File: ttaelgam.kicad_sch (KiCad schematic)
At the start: 32 parts, among them J1 Conn_01x04, J2 USB_C_Receptacle_USB2.0_16P, J3 Conn_01x05, SW1 SW_Push, SW2 SW_Push, U1 RP2040, U2 XC6206PxxxMR, U3 SRV05-4, U4 W25Q128JVS, Y1 Crystal_GND24

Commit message: 202408042026
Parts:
- added D1, D10, D11, D12, D13, D14, D15, D16, D17, D18, D19, D2, D20, D21, D22, D23, D24, D25, D26, D27, D28, D29, D3, D30, D31, D32, D33, D34, D35, D36, D37, D38, D39, D4, D40, D41, D42, D43, D44, D45, D46, D47, D48, D49, D5, D50, D51, D52, D53, D54, D55, D56, D57, D58, D59, D6, D60, D61, D62, D63, D64, D65, D66, D67, D68, D69, D7, D70, D71, D72, D73, D74, D75, D76, D77, D78, D79, D8, D80, D81, D82, D83, D84, D85, D86, D87, D88, D89, D9, D90: D_Small, Diode_SMD:D_SOD-123, symbol Device:D_Small
- added MX1, MX10, MX11, MX12, MX13, MX14, MX15, MX16, MX17, MX18, MX19, MX2, MX20, MX21, MX22, MX23, MX24, MX25, MX26, MX27, MX28, MX29, MX3, MX30, MX31, MX32, MX33, MX34, MX35, MX36, MX37, MX38, MX39, MX4, MX40, MX41, MX42, MX43, MX44, MX45, MX46, MX47, MX48, MX49, MX5, MX50, MX51, MX52, MX53, MX54, MX55, MX56, MX57, MX58, MX59, MX6, MX60, MX61, MX62, MX63, MX64, MX65, MX66, MX67, MX68, MX69, MX7, MX70, MX71, MX72, MX73, MX74, MX75, MX76, MX77, MX78, MX79, MX8, MX80, MX81, MX82, MX83, MX84, MX85, MX86, MX87, MX88, MX89, MX9, MX90: MX_SW_HS, marbastlib-mx:SW_MX_HS_CPG151101S11_1u, symbol marbastlib-mx:MX_SW_HS_CPG151101S11
- BOOT1: renamed from SW2; footprint (none) -> Button_Switch_SMD:SW_SPST_TL3342
- C1, C2: footprint (none) -> Capacitor_SMD:C_0402_1005Metric
- C10: renamed from C7; footprint (none) -> Capacitor_SMD:C_0402_1005Metric
- C11: renamed from C8; footprint (none) -> Capacitor_SMD:C_0402_1005Metric
- C12: renamed from C9; footprint (none) -> Capacitor_SMD:C_0402_1005Metric
- C3: renamed from C4; footprint (none) -> Capacitor_SMD:C_0402_1005Metric
- C4: renamed from C5; footprint (none) -> Capacitor_SMD:C_0402_1005Metric
- C5: renamed from C12; footprint (none) -> Capacitor_SMD:C_0402_1005Metric
- C6: renamed from C10; footprint (none) -> Capacitor_SMD:C_0402_1005Metric
- C7: renamed from C11; footprint (none) -> Capacitor_SMD:C_0402_1005Metric
- C8: renamed from C3; footprint (none) -> Capacitor_SMD:C_0603_1608Metric
- C9: renamed from C6; footprint (none) -> Capacitor_SMD:C_0402_1005Metric
- F1: renamed from F2; footprint (none) -> Fuse:Fuse_1206_3216Metric
- J1: renamed from J2; footprint (none) -> Connector_USB:USB_C_Receptacle_HRO_TYPE-C-31-M-12
- J2: renamed from J1; footprint (none) -> Connector_JST:JST_SH_SM04B-SRSS-TB_1x04-1MP_P1.00mm_Horizontal
- J3: footprint (none) -> Connector_PinHeader_2.54mm:PinHeader_1x05_P2.54mm_Vertical
- R1: renamed from R2; footprint (none) -> Resistor_SMD:R_0402_1005Metric
- R2: renamed from R1; footprint (none) -> Resistor_SMD:R_0402_1005Metric
- R3: renamed from R9; footprint (none) -> Resistor_SMD:R_0402_1005Metric
- R4: renamed from R3; footprint (none) -> Resistor_SMD:R_0402_1005Metric
- R5: renamed from R8; footprint (none) -> Resistor_SMD:R_0402_1005Metric
- R6: renamed from R7; footprint (none) -> Resistor_SMD:R_0402_1005Metric
- R7: renamed from R4; footprint (none) -> Resistor_SMD:R_0402_1005Metric
- R8: renamed from R5; footprint (none) -> Resistor_SMD:R_0402_1005Metric
- R9: renamed from R6; footprint (none) -> Resistor_SMD:R_0402_1005Metric
- RST1: renamed from SW1; footprint (none) -> Button_Switch_SMD:SW_SPST_TL3342
- Y1: footprint (none) -> Crystal:Crystal_SMD_3225-4Pin_3.2x2.5mm
- renumbered U2 to U1, U1 to U2
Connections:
- new net: D13.2 (A), MX13.2
- new net: D31.2 (A), MX31.2
- new net: D46.2 (A), MX46.2
- new net: D73.2 (A), MX73.2
- new net: D89.2 (A), MX89.2
- new net: D74.2 (A), MX74.2
- new net: D64.2 (A), MX64.2
- new net: D24.2 (A), MX24.2
- new net: D47.2 (A), MX47.2
- new net: D69.2 (A), MX69.2
- new net: D32.2 (A), MX32.2
- new net: D56.2 (A), MX56.2
- new net: D17.2 (A), MX17.2
- new net: D14.2 (A), MX14.2
- new net: D16.2 (A), MX16.2
- new net: D15.2 (A), MX15.2
- new net: D41.2 (A), MX41.2
- new net: D5.2 (A), MX5.2
- new net: D68.2 (A), MX68.2
- new net: D52.2 (A), MX52.2
- new net: D85.2 (A), MX85.2
- new net: D70.2 (A), MX70.2
- new net: D53.2 (A), MX53.2
- new net: D7.2 (A), MX7.2
- new net: D61.2 (A), MX61.2
- new net: D75.2 (A), MX75.2
- new net: D34.2 (A), MX34.2
- new net: D9.2 (A), MX9.2
- new net: D4.2 (A), MX4.2
- new net: D49.2 (A), MX49.2
- new net: D66.2 (A), MX66.2
- new net: D21.2 (A), MX21.2
- new net: D30.2 (A), MX30.2
- new net: D50.2 (A), MX50.2
- new net: D72.2 (A), MX72.2
- new net: D62.2 (A), MX62.2
- new net: D20.2 (A), MX20.2
- new net: D39.2 (A), MX39.2
- new net: D54.2 (A), MX54.2
- new net: D11.2 (A), MX11.2
- new net: D88.2 (A), MX88.2
- new net: D10.2 (A), MX10.2
- new net: D80.2 (A), MX80.2
- new net: D82.2 (A), MX82.2
- new net: D43.2 (A), MX43.2
- new net: D48.2 (A), MX48.2
- new net: D3.2 (A), MX3.2
- new net: D40.2 (A), MX40.2
- new net: D37.2 (A), MX37.2
- new net: D83.2 (A), MX83.2
- new net: D38.2 (A), MX38.2
- new net: D29.2 (A), MX29.2
- new net: D55.2 (A), MX55.2
- new net: D8.2 (A), MX8.2
- new net: D33.2 (A), MX33.2
- new net: D86.2 (A), MX86.2
- new net: D23.2 (A), MX23.2
- new net: D44.2 (A), MX44.2
- new net: D63.2 (A), MX63.2
- new net: D28.2 (A), MX28.2
- new net: D60.2 (A), MX60.2
- new net: D26.2 (A), MX26.2
- new net: D58.2 (A), MX58.2
- new net: D77.2 (A), MX77.2
- new net: D76.2 (A), MX76.2
- new net: D57.2 (A), MX57.2
- new net: D45.2 (A), MX45.2
- new net: D2.2 (A), MX2.2
- new net: D84.2 (A), MX84.2
- new net: D35.2 (A), MX35.2
- new net: D59.2 (A), MX59.2
- new net: D90.2 (A), MX90.2
- new net: D71.2 (A), MX71.2
- new net: D18.2 (A), MX18.2
- new net: D6.2 (A), MX6.2
- new net: D12.2 (A), MX12.2
- new net: D67.2 (A), MX67.2
- new net: D36.2 (A), MX36.2
- new net: D78.2 (A), MX78.2
- new net: D19.2 (A), MX19.2
- new net: D79.2 (A), MX79.2
- new net: D42.2 (A), MX42.2
- new net: D25.2 (A), MX25.2
- new net: D1.2 (A), MX1.2
- new net: D65.2 (A), MX65.2
- new net: D27.2 (A), MX27.2
- new net: D51.2 (A), MX51.2
- new net: D81.2 (A), MX81.2
- new net: D87.2 (A), MX87.2
- new net: D22.2 (A), MX22.2
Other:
- moved on the sheet: C1, C10, C11, C12, C2, C8, C9, J2, U1, U3

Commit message: 0804over
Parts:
- added S30: MX_stab, marbastlib-mx:STAB_MX_2u, symbol marbastlib-mx:MX_stab
- added S63, S64: MX_stab, marbastlib-mx:STAB_MX_2.25u, symbol marbastlib-mx:MX_stab
- added S76, S81: MX_stab, marbastlib-mx:STAB_MX_2.75u, symbol marbastlib-mx:MX_stab
- added S82: MX_stab, marbastlib-mx:STAB_MX_3u, symbol marbastlib-mx:MX_stab
- MX34, MX47: footprint marbastlib-mx:SW_MX_HS_CPG151101S11_1u -> marbastlib-mx:SW_MX_HS_CPG151101S11_1.5u
- MX51: footprint marbastlib-mx:SW_MX_HS_CPG151101S11_1u -> marbastlib-mx:SW_MX_HS_CPG151101S11_1.75u_STP_1.25
- MX78, MX79, MX80, MX83: footprint marbastlib-mx:SW_MX_HS_CPG151101S11_1u -> marbastlib-mx:SW_MX_HS_CPG151101S11_1.25u

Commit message: 20240807
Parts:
- added C13, C14, C15, C16: 100n, Capacitor_SMD:C_0402_1005Metric, symbol Device:C_Small
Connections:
- net +1V1: now also C16.1
- net +3V3: now also C13.1, C14.1, C15.1
- net GND: now also J3.1 (Pin_1), C13.2, C14.2, C15.2, C16.2; no longer J3.3 (Pin_3)
- net Q_CLK: now also U4.6 (CLK); no longer U4.7 (IO3)
- net Q_I00: now also U4.5 (DI(IO0)); no longer U4.6 (CLK)
- net Q_I01: now also U4.2 (DO(IO1)); no longer U4.5 (DI(IO0))
- net Q_I02: now also U4.1 (~{CS}); no longer U4.2 (DO(IO1))
- net Q_I03: now also U4.7 (IO3); no longer U4.3 (IO2)
- net Q_SEL: now also U4.3 (IO2); no longer U4.1 (~{CS})
- net RESET: now also J3.3 (Pin_3); no longer J3.1 (Pin_1)
- net SWC: now also J3.5 (Pin_5); no longer J3.4 (Pin_4)
- net SWD: now also J3.4 (Pin_4); no longer J3.5 (Pin_5)
- net at MX13.1: now also MX30.1, MX47.1, MX63.1, MX76.1, MX87.1
- net at MX31.1: now also MX14.1, MX48.1, MX88.1
- net at D46.1 (K): now also D34.1 (K), D35.1 (K), D36.1 (K), D37.1 (K), D38.1 (K), D39.1 (K), D40.1 (K), D41.1 (K), D42.1 (K), D43.1 (K), D44.1 (K), D45.1 (K), D47.1 (K), D48.1 (K), D49.1 (K), D50.1 (K)
- net at MX73.1: now also MX27.1, MX43.1, MX60.1, MX9.1
- net at MX89.1: now also MX15.1, MX32.1, MX49.1, MX77.1
- net at MX74.1: now also MX10.1, MX28.1, MX44.1, MX61.1
- net at D64.1 (K): now also D65.1 (K), D66.1 (K), D67.1 (K), D68.1 (K), D69.1 (K), D70.1 (K), D71.1 (K), D72.1 (K), D73.1 (K), D74.1 (K), D75.1 (K), D76.1 (K), D77.1 (K)
- net at MX24.1: now also MX40.1, MX57.1, MX6.1, MX70.1, MX82.1
- net at MX69.1: now also MX23.1
- net at D32.1 (K): now also D17.1 (K), D18.1 (K), D19.1 (K), D20.1 (K), D21.1 (K), D22.1 (K), D23.1 (K), D24.1 (K), D25.1 (K), D26.1 (K), D27.1 (K), D28.1 (K), D29.1 (K), D30.1 (K), D31.1 (K), D33.1 (K)
- net at D56.1 (K): now also D51.1 (K), D52.1 (K), D53.1 (K), D54.1 (K), D55.1 (K), D57.1 (K), D58.1 (K), D59.1 (K), D60.1 (K), D61.1 (K), D62.1 (K), D63.1 (K)
- net at D16.1 (K): now also D1.1 (K), D10.1 (K), D11.1 (K), D12.1 (K), D13.1 (K), D14.1 (K), D15.1 (K), D2.1 (K), D3.1 (K), D4.1 (K), D5.1 (K), D6.1 (K), D7.1 (K), D8.1 (K), D9.1 (K)
- net at D85.1 (K): now also D78.1 (K), D79.1 (K), D80.1 (K), D81.1 (K), D82.1 (K), D83.1 (K), D84.1 (K), D86.1 (K), D87.1 (K), D88.1 (K), D89.1 (K), D90.1 (K)
- net at MX53.1: now also MX19.1, MX3.1, MX36.1, MX66.1, MX80.1
- net at MX7.1: now also MX25.1, MX41.1, MX58.1, MX71.1, MX83.1
- net at MX75.1: now also MX11.1, MX29.1, MX45.1, MX62.1, MX85.1
- net at MX50.1: now also MX16.1, MX33.1, MX90.1
- net at MX52.1: now also MX18.1, MX2.1, MX35.1, MX65.1, MX79.1
- net at MX54.1: now also MX20.1, MX37.1, MX4.1, MX67.1, MX81.1
- net at MX39.1: now also MX22.1, MX56.1
- net at MX21.1: now also MX38.1, MX5.1, MX55.1, MX68.1
- net at MX26.1: now also MX42.1, MX59.1, MX72.1, MX8.1, MX84.1
- net at MX86.1: now also MX12.1, MX46.1
- net at MX17.1: now also MX1.1, MX34.1, MX51.1, MX64.1, MX78.1
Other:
- moved on the sheet: C10, C11, C12, C3, C4, C8, C9, D10, D11, D12, D13, D14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

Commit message: 20240808
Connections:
- net COL12: now reaches MX13.1, MX30.1, MX47.1, MX63.1, MX76.1, MX87.1
- net COL12: now also U2.11 (GPIO8)
- net COL13: now reaches MX14.1, MX31.1, MX48.1, MX88.1
- net COL13: now also U2.12 (GPIO9)
- net ROW2: now reaches D34.1 (K), D35.1 (K), D36.1 (K), D37.1 (K), D38.1 (K), D39.1 (K), D40.1 (K), D41.1 (K), D42.1 (K), D43.1 (K), D44.1 (K), D45.1 (K), D46.1 (K), D47.1 (K), D48.1 (K), D49.1 (K), D50.1 (K)
- net ROW2: now also U2.15 (GPIO12)
- net COL8: now reaches MX27.1, MX43.1, MX60.1, MX73.1, MX9.1
- net COL8: now also U2.6 (GPIO4)
- net COL14: now reaches MX15.1, MX32.1, MX49.1, MX77.1, MX89.1
- net COL14: now also U2.13 (GPIO10)
- net COL9: now reaches MX10.1, MX28.1, MX44.1, MX61.1, MX74.1
- net COL9: now also U2.7 (GPIO5)
- net ROW4: now reaches D64.1 (K), D65.1 (K), D66.1 (K), D67.1 (K), D68.1 (K), D69.1 (K), D70.1 (K), D71.1 (K), D72.1 (K), D73.1 (K), D74.1 (K), D75.1 (K), D76.1 (K), D77.1 (K)
- net ROW4: now also U2.27 (GPIO16)
- net COL5: now reaches MX24.1, MX40.1, MX57.1, MX6.1, MX70.1, MX82.1
- net COL17: now reaches MX23.1, MX69.1
- net ROW1: now reaches D17.1 (K), D18.1 (K), D19.1 (K), D20.1 (K), D21.1 (K), D22.1 (K), D23.1 (K), D24.1 (K), D25.1 (K), D26.1 (K), D27.1 (K), D28.1 (K), D29.1 (K), D30.1 (K), D31.1 (K), D32.1 (K), D33.1 (K)
- net ROW1: now also U2.16 (GPIO13)
- net ROW3: now reaches D51.1 (K), D52.1 (K), D53.1 (K), D54.1 (K), D55.1 (K), D56.1 (K), D57.1 (K), D58.1 (K), D59.1 (K), D60.1 (K), D61.1 (K), D62.1 (K), D63.1 (K)
- net ROW3: now also U2.28 (GPIO17)
- net ROW0: now reaches D1.1 (K), D10.1 (K), D11.1 (K), D12.1 (K), D13.1 (K), D14.1 (K), D15.1 (K), D16.1 (K), D2.1 (K), D3.1 (K), D4.1 (K), D5.1 (K), D6.1 (K), D7.1 (K), D8.1 (K), D9.1 (K)
- net ROW0: now also U2.17 (GPIO14)
- net ROW5: now reaches D78.1 (K), D79.1 (K), D80.1 (K), D81.1 (K), D82.1 (K), D83.1 (K), D84.1 (K), D85.1 (K), D86.1 (K), D87.1 (K), D88.1 (K), D89.1 (K), D90.1 (K)
- net ROW5: now also U2.18 (GPIO15)
- net COL2: now reaches MX19.1, MX3.1, MX36.1, MX53.1, MX66.1, MX80.1
- net COL6: now reaches MX25.1, MX41.1, MX58.1, MX7.1, MX71.1, MX83.1
- net COL10: now reaches MX11.1, MX29.1, MX45.1, MX62.1, MX75.1, MX85.1
- net COL10: now also U2.8 (GPIO6)
- net COL15: now reaches MX16.1, MX33.1, MX50.1, MX90.1
- net COL15: now also U2.14 (GPIO11)
- net COL1: now reaches MX18.1, MX2.1, MX35.1, MX52.1, MX65.1, MX79.1
- net COL3: now reaches MX20.1, MX37.1, MX4.1, MX54.1, MX67.1, MX81.1
- net COL11: now reaches U2.9 (GPIO7)
- net COL11: now also MX12.1, MX46.1, MX86.1
- net COL16: now reaches MX22.1, MX39.1, MX56.1
- net COL4: now reaches MX21.1, MX38.1, MX5.1, MX55.1, MX68.1
- net COL7: now reaches MX26.1, MX42.1, MX59.1, MX72.1, MX8.1, MX84.1
- net COL0: now reaches MX1.1, MX17.1, MX34.1, MX51.1, MX64.1, MX78.1

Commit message: 0810
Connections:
- net COL0: now also U2.36 (GPIO24)
- net COL1: now also U2.35 (GPIO23)
- net COL16: now also U2.30 (GPIO19)
- net COL17: now also U2.29 (GPIO18)
- net COL2: now also U2.34 (GPIO22)
- net COL3: now also U2.32 (GPIO21)
- net COL4: now also U2.31 (GPIO20)
- net COL5: now also U2.3 (GPIO1)
- net COL6: now also U2.4 (GPIO2)
- net COL7: now also U2.5 (GPIO3)
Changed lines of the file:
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@@
+		)
+	)
+	(global_label "COL5"
+		(shape input)
+		(at 85.09 147.32 0)
+		(fields_autoplaced yes)
+		(effects
+			(font
+				(size 1.27 1.27)
+			)
+			(justify left)
+		)
+		(property "Intersheetrefs" "${INTERSHEET_REFS}"
+			(at 92.9133 147.32 0)
+			(effects
+				(font
+					(size 1.27 1.27)
+				)
+				(justify left)
+				(hide yes)
+			)
 		)
 	)
@@
 		)
 	)
+	(global_label "COL0"
+		(shape input)
+		(at 85.09 205.74 0)
+		(fields_autoplaced yes)
+		(effects
+			(font
+				(size 1.27 1.27)
+			)
+			(justify left)
+		)
+		(property "Intersheetrefs" "${INTERSHEET_REFS}"
+			(at 92.9133 205.74 0)
+			(effects
+				(font
+					(size 1.27 1.27)
+				)
+				(justify left)
+				(hide yes)
+			)
+		)
+	)
 	(global_label "Q_SEL"
 		(shape input)
@@
 		)
 	)
+	(global_label "COL3"
+		(shape input)
+		(at 85.09 198.12 0)
+		(fields_autoplaced yes)
+		(effects
+			(font
+				(size 1.27 1.27)
+			)
+			(justify left)
+		)
+		(property "Intersheetrefs" "${INTERSHEET_REFS}"
+			(at 92.9133 198.12 0)
+			(effects
+				(font
+					(size 1.27 1.27)
+				)
+				(justify left)
+				(hide yes)
+			)
+		)
+	)
 	(global_label "COL6"
 		(shape input)
@@
 		)
 	)
+	(global_label "COL4"
+		(shape input)
+		(at 85.09 195.58 0)
+		(fields_autoplaced yes)
+		(effects
+			(font
+				(size 1.27 1.27)
+			)
+			(justify left)
+		)
+		(property "Intersheetrefs" "${INTERSHEET_REFS}"
+			(at 92.9133 195.58 0)
+			(effects
+				(font
+					(size 1.27 1.27)
+				)
+				(justify left)
+				(hide yes)
+			)
+		)
+	)
 	(global_label "RESET"
 		(shape input)
@@
 		)
 	)
+	(global_label "COL1"
+		(shape input)
+		(at 85.09 203.2 0)
+		(fields_autoplaced yes)
+		(effects
+			(font
+				(size 1.27 1.27)
+			)
+			(justify left)
+		)
+		(property "Intersheetrefs" "${INTERSHEET_REFS}"
+			(at 92.9133 203.2 0)
+			(effects
+				(font
+					(size 1.27 1.27)
+				)
+				(justify left)
+				(hide yes)
+			)
+		)
+	)
 	(global_label "ROW4"
 		(shape input)
@@
 		)
 	)
+	(global_label "COL7"
+		(shape input)
+		(at 85.09 152.4 0)
+		(fields_autoplaced yes)
+		(effects
+			(font
+				(size 1.27 1.27)
+			)
+			(justify left)
+		)
+		(property "Intersheetrefs" "${INTERSHEET_REFS}"
+			(at 92.9133 152.4 0)
+			(effects
+				(font
+					(size 1.27 1.27)
+				)
+				(justify left)
+				(hide yes)
+			)
+		)
+	)
 	(global_label "COL5"
 		(shape input)
@@
 		)
 	)
+	(global_label "COL17"
+		(shape input)
+		(at 85.09 190.5 0)
+		(fields_autoplaced yes)
+		(effects
+			(font
+				(size 1.27 1.27)
+			)
+			(justify left)
+		)
+		(property "Intersheetrefs" "${INTERSHEET_REFS}"
+			(at 94.1228 190.5 0)
+			(effects
+				(font
+					(size 1.27 1.27)
+				)
+				(justify left)
+				(hide yes)
+			)
+		)
+	)
+	(global_label "COL16"
+		(shape input)
+		(at 85.09 193.04 0)
+		(fields_autoplaced yes)
+		(effects
+			(font
+				(size 1.27 1.27)
+			)
+			(justify left)
+		)
+		(property "Intersheetrefs" "${INTERSHEET_REFS}"
+			(at 94.1228 193.04 0)
+			(effects
+				(font
+					(size 1.27 1.27)
+				)
+				(justify left)
+				(hide yes)
+			)
+		)
+	)
 	(global_label "COL15"
 		(shape input)
@@
 		)
 	)
+	(global_label "COL6"
+		(shape input)
+		(at 85.09 149.86 0)
+		(fields_autoplaced yes)
+		(effects
+			(font
+				(size 1.27 1.27)
+			)
+			(justify left)
+		)
+		(property "Intersheetrefs" "${INTERSHEET_REFS}"
+			(at 92.9133 149.86 0)
+			(effects
+				(font
+					(size 1.27 1.27)
+				)
+				(justify left)
+				(hide yes)
+			)
+		)
+	)
 	(global_label "RESET"
 		(shape input)
@@
 				(hide yes)
 			)
+		)
+	)
+	(global_label "COL2"
+		(shape input)
+		(at 85.09 200.66 0)
+		(fields_autoplaced yes)
+		(effects
+			(font
+				(size 1.27 1.27)
+			)
+			(justify left)
+		)
+		(property "Intersheetrefs" "${INTERSHEET_REFS}"
+			(at 92.9133 200.66 0)
+			(effects
+				(font
+					(size 1.27 1.27)
+				)
+				(justify left)
+				(hide yes)
+			)

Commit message: 0817
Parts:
- added J4: 78171-0004, Connector_Molex:Molex_Pico-EZmate_78171-0004_1x04-1MP_P1.20mm_Vertical, symbol Connector_Generic_MountingPin:Conn_01x04_MountingPin
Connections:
- net +5V: now also J4.1 (Pin_1)
- net D+: now also J4.3 (Pin_3)
- net D-: now also J4.2 (Pin_2)
- net GND: now also J4.4 (Pin_4), J4.MP (MountPin)
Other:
- moved on the sheet: C1, C2, J2, U1

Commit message: 0901
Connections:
- net COL0: now also U2.7 (GPIO5); no longer U2.36 (GPIO24)
- net COL1: now also U2.8 (GPIO6); no longer U2.35 (GPIO23)
- net COL10: now also U2.35 (GPIO23); no longer U2.8 (GPIO6)
- net COL11: now also U2.36 (GPIO24); no longer U2.9 (GPIO7)
- net COL12: now also U2.37 (GPIO25); no longer U2.11 (GPIO8)
- net COL13: now also U2.38 (GPIO26_ADC0); no longer U2.12 (GPIO9)
- net COL14: now also U2.39 (GPIO27_ADC1); no longer U2.13 (GPIO10)
- net COL15: now also U2.40 (GPIO28_ADC2); no longer U2.14 (GPIO11)
- net COL16: now also U2.13 (GPIO10); no longer U2.30 (GPIO19)
- net COL17: now also U2.14 (GPIO11); no longer U2.29 (GPIO18)
- net COL2: now also U2.9 (GPIO7); no longer U2.34 (GPIO22)
- net COL3: now also U2.11 (GPIO8); no longer U2.32 (GPIO21)
- net COL4: now also U2.12 (GPIO9); no longer U2.31 (GPIO20)
- net COL5: now also U2.29 (GPIO18); no longer U2.3 (GPIO1)
- net COL6: now also U2.30 (GPIO19); no longer U2.4 (GPIO2)
- net COL7: now also U2.31 (GPIO20); no longer U2.5 (GPIO3)
- net COL8: now also U2.32 (GPIO21); no longer U2.6 (GPIO4)
- net COL9: now also U2.34 (GPIO22); no longer U2.7 (GPIO5)
- net ROW0: now also U2.16 (GPIO13); no longer U2.17 (GPIO14)
- net ROW1: now also U2.17 (GPIO14); no longer U2.16 (GPIO13)
- net ROW2: now also U2.18 (GPIO15); no longer U2.15 (GPIO12)
- net ROW5: now also U2.2 (GPIO0); no longer U2.18 (GPIO15)

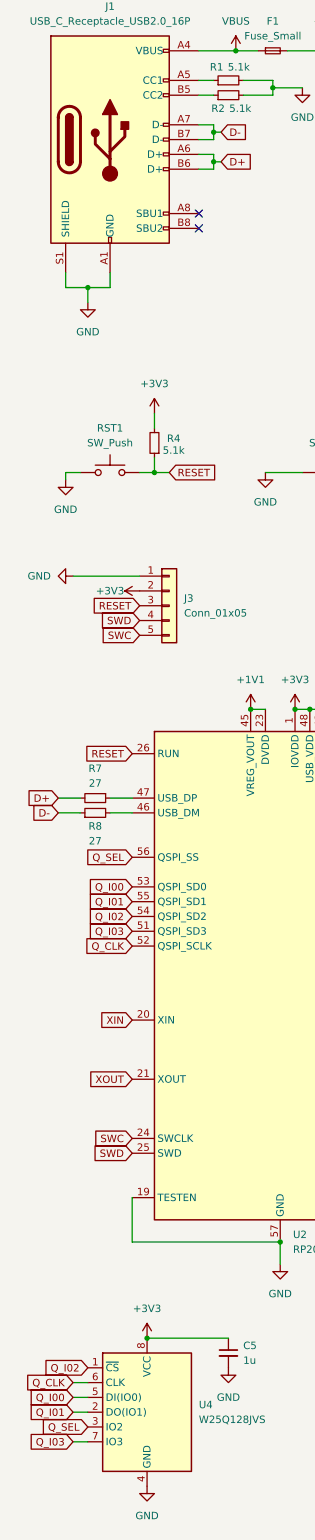
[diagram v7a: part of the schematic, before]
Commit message: Problem
Problem

-Crystal Unit 12MHz
-Flash wiring error
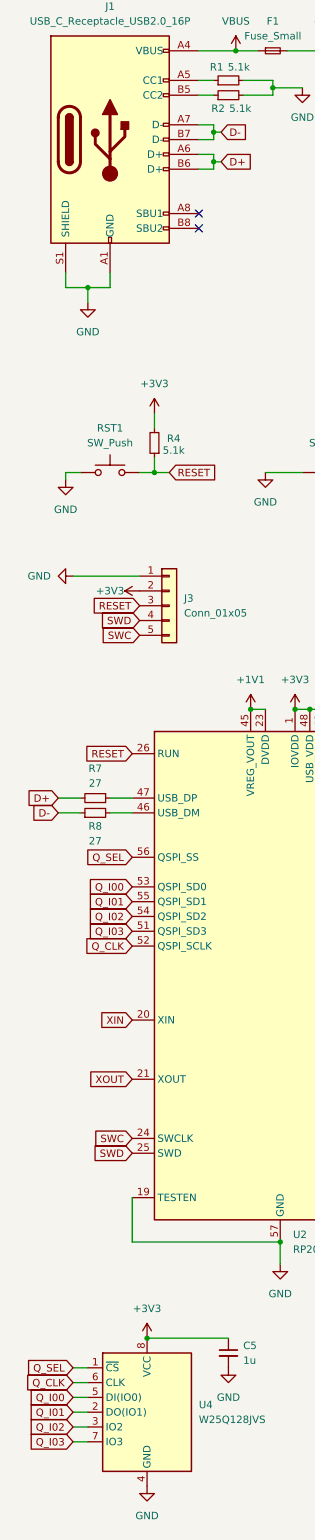
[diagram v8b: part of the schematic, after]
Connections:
- net Q_I02: now also U4.3 (IO2); no longer U4.1 (~{CS})
- net Q_SEL: now also U4.1 (~{CS}); no longer U4.3 (IO2)
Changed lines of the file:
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@@
 (kicad_sch
-	(version 20231120)
+	(version 20250114)
 	(generator "eeschema")
-	(generator_version "8.0")
+	(generator_version "9.0")
 	(paper "A3")
 	(junction
@@
 	(wire
 		(pts
+			(xy 24.13 260.35) (xy 26.67 260.35)
+		)
+		(stroke
+			(width 0)
+			(type default)
+		)
+	)
+	(wire
+		(pts
 			(xy 105.41 133.35) (xy 105.41 156.21)
 		)
@@
 	(wire
 		(pts
+			(xy 24.13 250.19) (xy 26.67 250.19)
+		)
+		(stroke
+			(width 0)
+			(type default)
+		)
+	)
+	(wire
+		(pts
 			(xy 49.53 43.18) (xy 48.26 43.18)
 		)
@@
 	(global_label "Q_SEL"
 		(shape input)
-		(at 26.67 260.35 180)
+		(at 24.13 250.19 180)
 		(fields_autoplaced yes)
 		(effects
@@
 		)
 		(property "Intersheetrefs" "${INTERSHEET_REFS}"
-			(at 18.0001 260.35 0)
+			(at 15.4601 250.19 0)
 			(effects
 				(font
@@
 	(global_label "Q_I02"
 		(shape input)
-		(at 26.67 250.19 180)
+		(at 24.13 260.35 180)
 		(fields_autoplaced yes)
 		(effects
@@
 		)
 		(property "Intersheetrefs" "${INTERSHEET_REFS}"
-			(at 18.3629 250.19 0)
+			(at 15.8229 260.35 0)
 			(effects
 				(font
@@
 		)
 	)
+	(embedded_fonts no)
 )
